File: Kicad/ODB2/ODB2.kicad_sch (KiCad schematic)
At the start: 31 parts, among them U1 STM32F412ZGTx

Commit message: ajout footprints
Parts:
- RST_C1: footprint (none) -> Capacitor_SMD:C_0805_2012Metric
- RST_R1: footprint (none) -> Resistor_SMD:R_0805_2012Metric
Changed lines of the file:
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@@
 			)
 		)
-		(property "Footprint" ""
+		(property "Footprint" "Resistor_SMD:R_0805_2012Metric"
 			(at 144.272 49.53 90)
 			(effects
@@
 			)
 		)
-		(property "Footprint" ""
+		(property "Footprint" "Capacitor_SMD:C_0805_2012Metric"
 			(at 147.0152 64.77 0)
 			(effects

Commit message: revision logic
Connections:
- net Pyros_DrogueOn renamed Pyros_DrogueODB
- net Pyros_MainOn renamed Pyros_MainODB
- net Pyros_Test renamed ~Pyros_Test

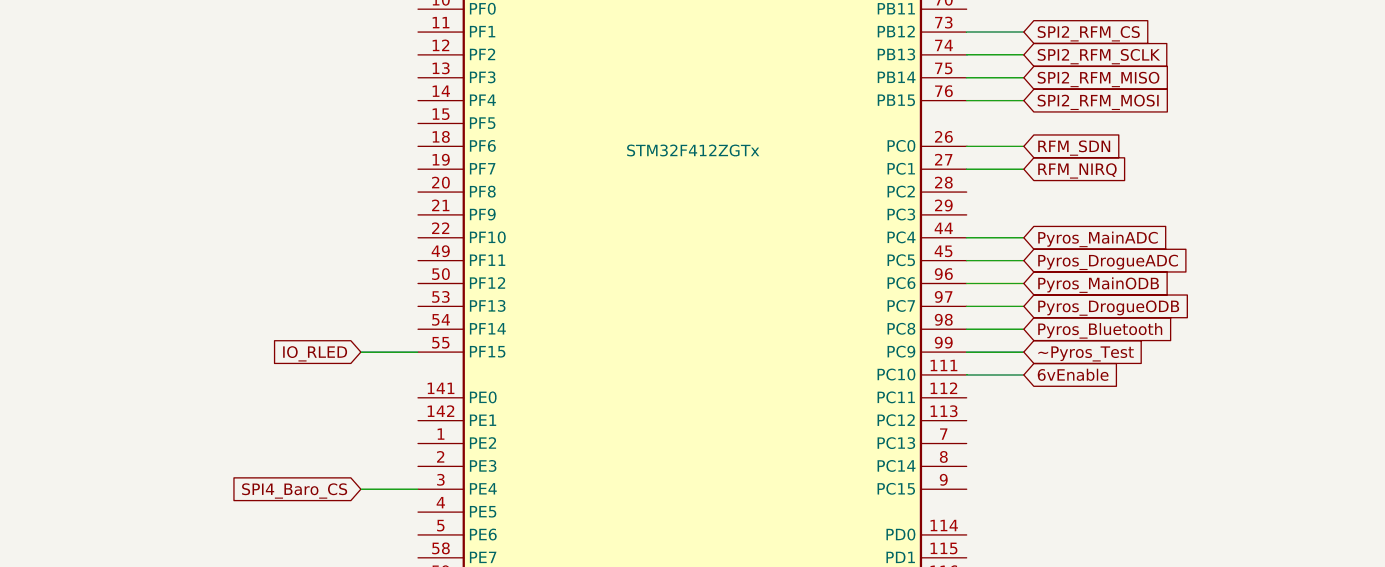
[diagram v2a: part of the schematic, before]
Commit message: ajout lecture tension batteries 1s / 2s
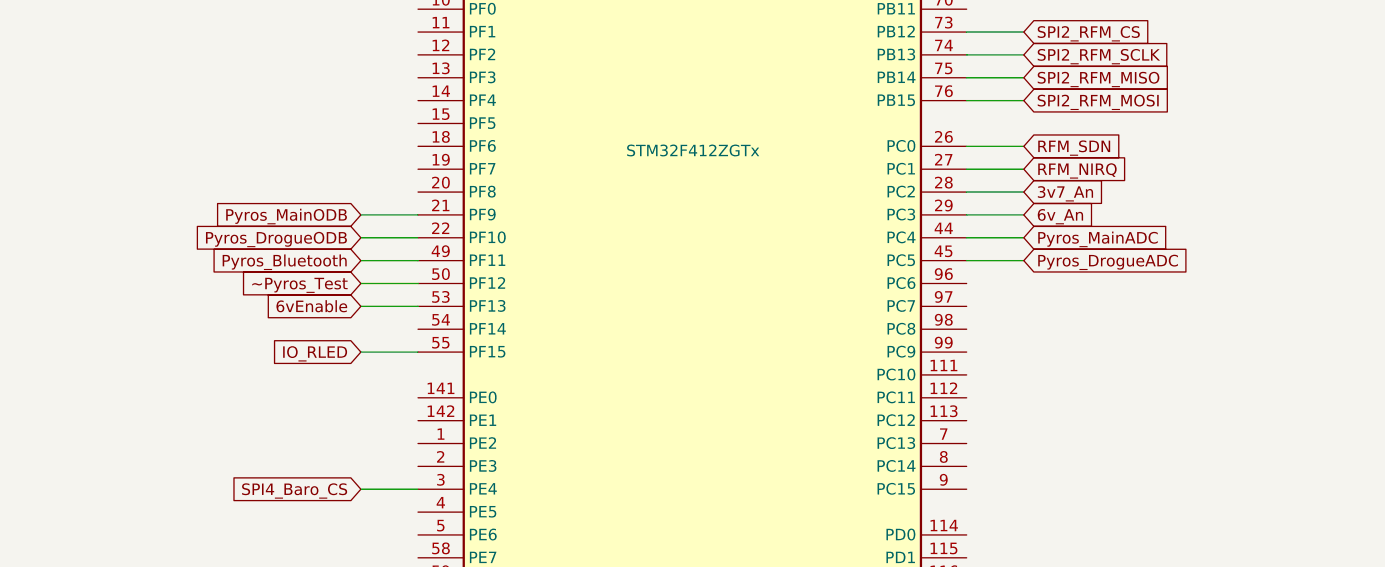
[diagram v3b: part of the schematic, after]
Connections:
- net 6vEnable: now also U1.53 (PF13); no longer U1.111 (PC10)
- net Pyros_Bluetooth: now also U1.49 (PF11); no longer U1.98 (PC8)
- net Pyros_DrogueODB: now also U1.22 (PF10); no longer U1.97 (PC7)
- net Pyros_MainODB: now also U1.21 (PF9); no longer U1.96 (PC6)
- net ~Pyros_Test: now also U1.50 (PF12); no longer U1.99 (PC9)
- net 3v7_An: now reaches U1.28 (PC2)
- net 6v_An: now reaches U1.29 (PC3)
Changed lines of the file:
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@@
-	(wire
-		(pts
-			(xy 231.14 162.56) (xy 237.49 162.56)
-		)
-		(stroke
-			(width 0)
-			(type default)
-		)
-	)
 	(wire
 		(pts
@@
 	(wire
 		(pts
+			(xy 231.14 149.86) (xy 237.49 149.86)
+		)
+		(stroke
+			(width 0)
+			(type default)
+		)
+	)
+	(wire
+		(pts
 			(xy 298.45 144.78) (xy 313.69 144.78)
 		)
@@
 	(wire
 		(pts
+			(xy 163.83 157.48) (xy 170.18 157.48)
+		)
+		(stroke
+			(width 0)
+			(type default)
+		)
+	)
+	(wire
+		(pts
 			(xy 375.92 139.7) (xy 375.92 142.24)
 		)
@@
 	(wire
 		(pts
+			(xy 231.14 147.32) (xy 237.49 147.32)
+		)
+		(stroke
+			(width 0)
+			(type default)
+		)
+	)
+	(wire
+		(pts
 			(xy 231.14 198.12) (xy 238.76 198.12)
 		)
@@
 	(wire
 		(pts
+			(xy 163.83 160.02) (xy 170.18 160.02)
+		)
+		(stroke
+			(width 0)
+			(type default)
+		)
+	)
+	(wire
+		(pts
 			(xy 163.83 180.34) (xy 170.18 180.34)
 		)
@@
 	(wire
 		(pts
-			(xy 231.14 160.02) (xy 237.49 160.02)
-		)
-		(stroke
-			(width 0)
-			(type default)
-		)
-	)
-	(wire
-		(pts
 			(xy 360.68 78.74) (xy 346.71 78.74)
 		)
@@
 	(wire
 		(pts
+			(xy 163.83 154.94) (xy 170.18 154.94)
+		)
+		(stroke
+			(width 0)
+			(type default)
+		)
+	)
+	(wire
+		(pts
 			(xy 388.62 31.75) (xy 392.43 31.75)
 		)
@@
 	(wire
 		(pts
-			(xy 231.14 165.1) (xy 237.49 165.1)
-		)
-		(stroke
-			(width 0)
-			(type default)
-		)
-	)
-	(wire
-		(pts
 			(xy 375.92 31.75) (xy 378.46 31.75)
 		)
@@
 	(wire
 		(pts
+			(xy 163.83 152.4) (xy 170.18 152.4)
+		)
+		(stroke
+			(width 0)
+			(type default)
+		)
+	)
+	(wire
+		(pts
 			(xy 360.68 66.04) (xy 346.71 66.04)
 		)
@@
 	(wire
 		(pts
+			(xy 163.83 149.86) (xy 170.18 149.86)
+		)
+		(stroke
+			(width 0)
+			(type default)
+		)
+	)
+	(wire
+		(pts
 			(xy 231.14 101.6) (xy 237.49 101.6)
 		)
@@
 	(wire
 		(pts
-			(xy 231.14 157.48) (xy 237.49 157.48)
-		)
-		(stroke
-			(width 0)
-			(type default)
-		)
-	)
-	(wire
-		(pts
 			(xy 300.99 88.9) (xy 316.23 88.9)
 		)
@@
 		(pts
 			(xy 316.23 99.06) (xy 316.23 101.6)
-		)
-		(stroke
-			(width 0)
-			(type default)
-		)
-	)
-	(wire
-		(pts
-			(xy 231.14 167.64) (xy 237.49 167.64)
 		)
 		(stroke
@@
 	(global_label "6vEnable"
 		(shape input)
-		(at 237.49 167.64 0)
-		(fields_autoplaced yes)
-		(effects
-			(font
-				(size 1.27 1.27)
-			)
-			(justify left)
-		)
-		(property "Intersheetrefs" "${INTERSHEET_REFS}"
-			(at 249.0021 167.64 0)
-			(effects
-				(font
-					(size 1.27 1.27)
-				)
-				(justify left)
+		(at 163.83 160.02 180)
+		(fields_autoplaced yes)
+		(effects
+			(font
+				(size 1.27 1.27)
+			)
+			(justify right)
+		)
+		(property "Intersheetrefs" "${INTERSHEET_REFS}"
+			(at 152.3179 160.02 0)
+			(effects
+				(font
+					(size 1.27 1.27)
+				)
+				(justify right)
 				(hide yes)
 			)
@@
 	(global_label "~Pyros_Test"
 		(shape input)
-		(at 237.49 165.1 0)
-		(fields_autoplaced yes)
-		(effects
-			(font
-				(size 1.27 1.27)
-			)
-			(justify left)
-		)
-		(property "Intersheetrefs" "${INTERSHEET_REFS}"
-			(at 251.3608 165.1 0)
-			(effects
-				(font
-					(size 1.27 1.27)
-				)
-				(justify left)
+		(at 163.83 157.48 180)
+		(fields_autoplaced yes)
+		(effects
+			(font
+				(size 1.27 1.27)
+			)
+			(justify right)
+		)
+		(property "Intersheetrefs" "${INTERSHEET_REFS}"
+			(at 149.9592 157.48 0)
+			(effects
+				(font
+					(size 1.27 1.27)
+				)
+				(justify right)
 				(hide yes)
 			)
@@
 		)
 	)
+	(global_label "3v7_An"
+		(shape input)
+		(at 237.49 147.32 0)
+		(fields_autoplaced yes)
+		(effects
+			(font
+				(size 1.27 1.27)
+			)
+			(justify left)
+		)
+		(property "Intersheetrefs" "${INTERSHEET_REFS}"
+			(at 247.067 147.32 0)
+			(effects
+				(font
+					(size 1.27 1.27)
+				)
+				(justify left)
+				(hide yes)
+			)
+		)
+	)
 	(global_label "SPI_ICM_CS"
 		(shape input)
@@
 	(global_label "Pyros_MainODB"
 		(shape input)
-		(at 237.49 157.48 0)
-		(fields_autoplaced yes)
-		(effects
-			(font
-				(size 1.27 1.27)
-			)
-			(justify left)
-		)
-		(property "Intersheetrefs" "${INTERSHEET_REFS}"
-			(at 254.8684 157.48 0)
+		(at 163.83 149.86 180)
+		(fields_autoplaced yes)
+		(effects
+			(font
+				(size 1.27 1.27)
+			)
+			(justify right)
+		)
+		(property "Intersheetrefs" "${INTERSHEET_REFS}"
+			(at 146.4516 149.86 0)
+			(effects
+				(font
+					(size 1.27 1.27)
+				)
+				(justify right)
+				(hide yes)
+			)
+		)
+	)
+	(global_label "6v_An"
+		(shape input)
+		(at 237.49 149.86 0)
+		(fields_autoplaced yes)
+		(effects
+			(font
+				(size 1.27 1.27)
+			)
+			(justify left)
+		)
+		(property "Intersheetrefs" "${INTERSHEET_REFS}"
+			(at 245.8575 149.86 0)
 			(effects
 				(font
@@
 	(global_label "Pyros_DrogueODB"
 		(shape input)
-		(at 237.49 160.02 0)
-		(fields_autoplaced yes)
-		(effects
-			(font
-				(size 1.27 1.27)
-			)
-			(justify left)
-		)
-		(property "Intersheetrefs" "${INTERSHEET_REFS}"
-			(at 257.106 160.02 0)
-			(effects
-				(font
-					(size 1.27 1.27)
-				)
-				(justify left)
+		(at 163.83 152.4 180)
+		(fields_autoplaced yes)
+		(effects
+			(font
+				(size 1.27 1.27)
+			)
+			(justify right)
+		)
+		(property "Intersheetrefs" "${INTERSHEET_REFS}"
+			(at 144.214 152.4 0)
+			(effects
+				(font
+					(size 1.27 1.27)
+				)
+				(justify right)
 				(hide yes)
 			)
@@
 	(global_label "Pyros_Bluetooth"
 		(shape input)
-		(at 237.49 162.56 0)
-		(fields_autoplaced yes)
-		(effects
-			(font
-				(size 1.27 1.27)
-			)
-			(justify left)
-		)
-		(property "Intersheetrefs" "${INTERSHEET_REFS}"
-			(at 255.7149 162.56 0)
-			(effects
-				(font
-					(size 1.27 1.27)
-				)
-				(justify left)
-				(hide yes)
-			)
+		(at 163.83 154.94 180)
+		(fields_autoplaced yes)
+		(effects
+			(font
+				(size 1.27 1.27)
+			)
+			(justify right)
+		)
+		(property "Intersheetrefs" "${INTERSHEET_REFS}"
+			(at 145.6051 154.94 0)
+			(effects
+				(font
+					(size 1.27 1.27)
+				)
+				(justify right)
+				(hide yes)
+			)

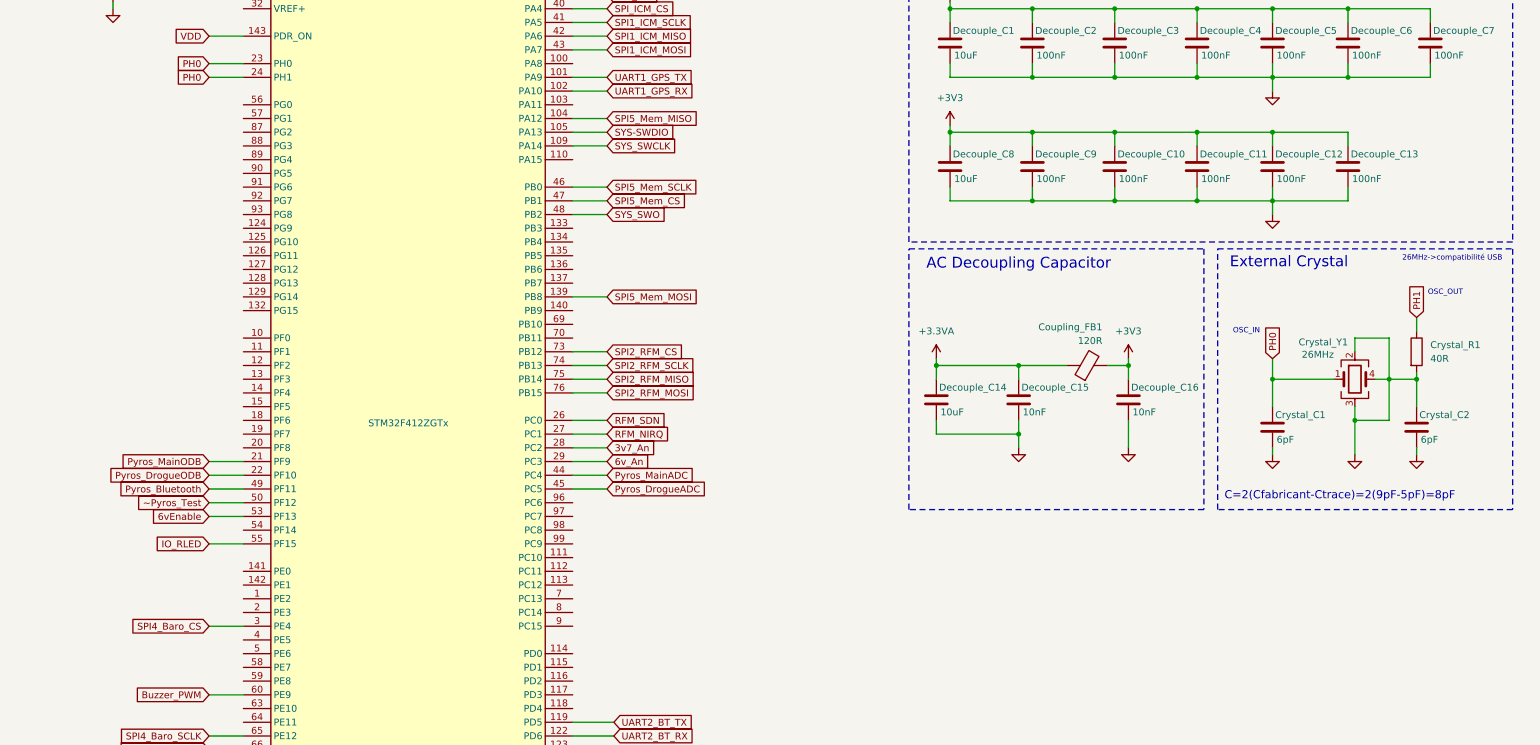
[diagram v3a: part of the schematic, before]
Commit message: ajout usbdata stm32 + modification pinout spi5_miso
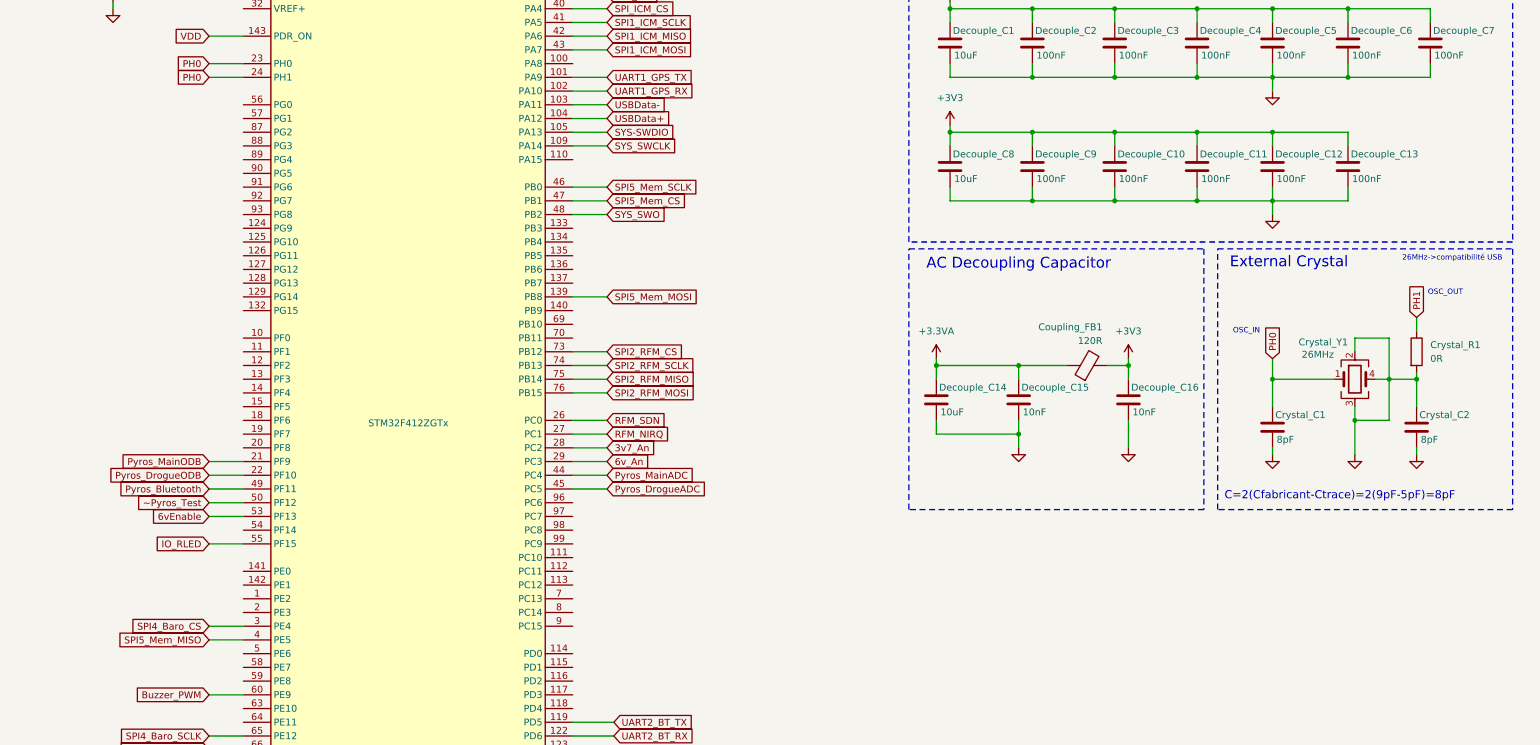
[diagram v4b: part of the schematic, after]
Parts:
- Crystal_C1, Crystal_C2: value 6pF -> 8pF
- Crystal_R1: value 40R -> 0R
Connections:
- net SPI5_Mem_MISO: now also U1.4 (PE5); no longer U1.104 (PA12)
- net USBData-: now reaches U1.103 (PA11)
- new net USBData+: U1.104 (PA12)
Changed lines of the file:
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@@
 	(wire
 		(pts
+			(xy 231.14 86.36) (xy 237.49 86.36)
+		)
+		(stroke
+			(width 0)
+			(type default)
+		)
+	)
+	(wire
+		(pts
 			(xy 360.68 88.9) (xy 346.71 88.9)
 		)
@@
 	(wire
 		(pts
+			(xy 231.14 83.82) (xy 237.49 83.82)
+		)
+		(stroke
+			(width 0)
+			(type default)
+		)
+	)
+	(wire
+		(pts
 			(xy 231.14 91.44) (xy 237.49 91.44)
 		)
@@
 	(wire
 		(pts
+			(xy 163.83 182.88) (xy 170.18 182.88)
+		)
+		(stroke
+			(width 0)
+			(type default)
+		)
+	)
+	(wire
+		(pts
 			(xy 139.7 55.88) (xy 146.05 55.88)
 		)
@@
 	(wire
 		(pts
-			(xy 231.14 86.36) (xy 237.49 86.36)
-		)
-		(stroke
-			(width 0)
-			(type default)
-		)
-	)
-	(wire
-		(pts
 			(xy 313.69 132.08) (xy 298.45 132.08)
 		)
@@
 	(global_label "SPI5_Mem_MISO"
 		(shape input)
-		(at 237.49 86.36 0)
+		(at 163.83 182.88 180)
 		(fields_autoplaced yes)
 		(effects
@@
 				(size 1.27 1.27)
 			)
-			(justify left)
+			(justify right)
 		)
 		(property "Intersheetrefs" "${INTERSHEET_REFS}"
-			(at 255.5337 86.36 0)
+			(at 145.7863 182.88 0)
 			(effects
 				(font
 					(size 1.27 1.27)
 				)
-				(justify left)
+				(justify right)
 				(hide yes)
 			)
@@
 		)
 	)
+	(global_label "USBData-"
+		(shape input)
+		(at 237.49 83.82 0)
+		(fields_autoplaced yes)
+		(effects
+			(font
+				(size 1.27 1.27)
+			)
+			(justify left)
+		)
+		(property "Intersheetrefs" "${INTERSHEET_REFS}"
+			(at 250.1513 83.82 0)
+			(effects
+				(font
+					(size 1.27 1.27)
+				)
+				(justify left)
+				(hide yes)
+			)
+		)
+	)
 	(global_label "SPI5_Mem_MOSI"
 		(shape input)
@@
 		)
 	)
+	(global_label "USBData+"
+		(shape input)
+		(at 237.49 86.36 0)
+		(fields_autoplaced yes)
+		(effects
+			(font
+				(size 1.27 1.27)
+			)
+			(justify left)
+		)
+		(property "Intersheetrefs" "${INTERSHEET_REFS}"
+			(at 250.1513 86.36 0)
+			(effects
+				(font
+					(size 1.27 1.27)
+				)
+				(justify left)
+				(hide yes)
+			)
+		)
+	)
 	(global_label "SYS_SWCLK"
 		(shape input)
@@
 			)
 		)
-		(property "Value" "6pF"
+		(property "Value" "8pF"
 			(at 361.442 145.796 0)
 			(effects
@@
 			)
 		)
-		(property "Value" "6pF"
+		(property "Value" "8pF"
 			(at 388.112 145.796 0)
 			(effects
@@
 			)
 		)
-		(property "Value" "40R"
+		(property "Value" "0R"
 			(at 389.89 130.8099 0)
 			(effects

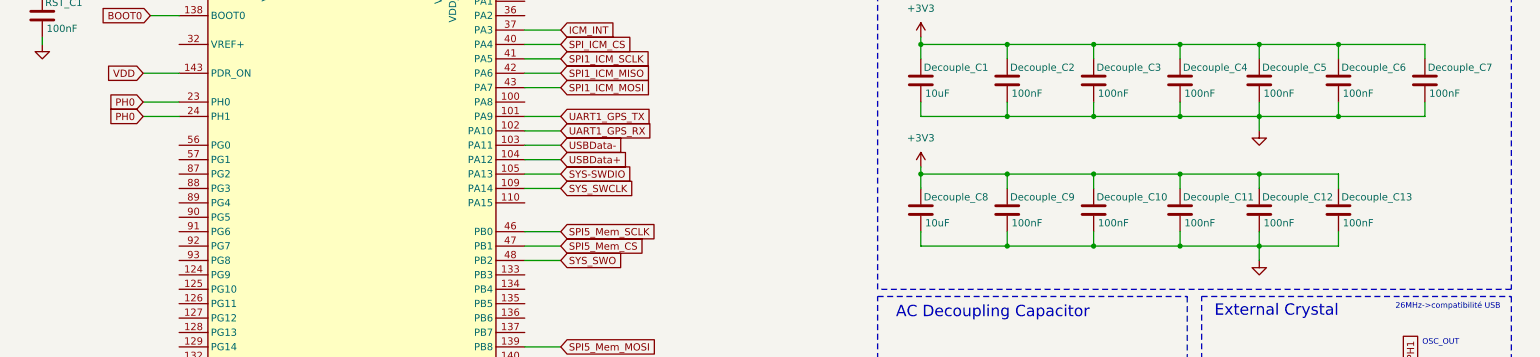
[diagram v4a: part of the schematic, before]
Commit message: fix label crystal + capacité découplage fix + add mosfet 6v isolation footprint
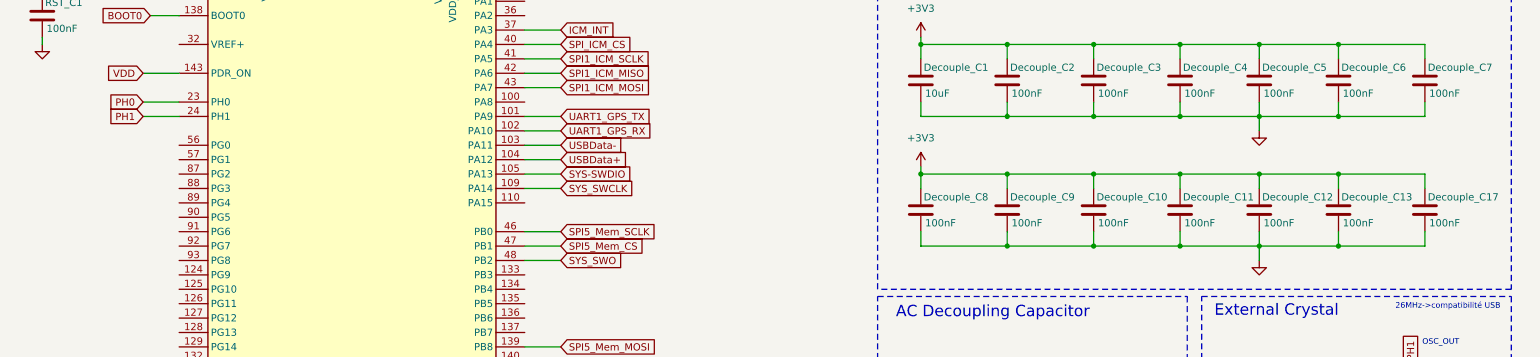
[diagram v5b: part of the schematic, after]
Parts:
- added Decouple_C17: 100nF, Capacitor_SMD:C_0805_2012Metric, symbol Device:C
- Decouple_C8: value 10uF -> 100nF
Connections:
- net +3V3: now also Decouple_C17.1
- net GND: now also Decouple_C17.2
- net PH0: no longer U1.24 (PH1)
- net PH1: now also U1.24 (PH1)
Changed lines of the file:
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@@
 	)
 	(junction
+		(at 374.65 88.9)
+		(diameter 0)
+		(color 0 0 0 0)
+	)
+	(junction
 		(at 387.35 134.62)
 		(diameter 0)
@@
 	)
 	(junction
+		(at 374.65 101.6)
+		(diameter 0)
+		(color 0 0 0 0)
+	)
+	(junction
 		(at 374.65 66.04)
 		(diameter 0)
@@
 	(wire
 		(pts
+			(xy 374.65 101.6) (xy 389.89 101.6)
+		)
+		(stroke
+			(width 0)
+			(type default)
+		)
+	)
+	(wire
+		(pts
 			(xy 213.36 44.45) (xy 210.82 44.45)
 		)
@@
 	(wire
 		(pts
+			(xy 389.89 99.06) (xy 389.89 101.6)
+		)
+		(stroke
+			(width 0)
+			(type default)
+		)
+	)
+	(wire
+		(pts
 			(xy 203.2 233.68) (xy 203.2 236.22)
 		)
@@
 	(wire
 		(pts
+			(xy 389.89 88.9) (xy 389.89 91.44)
+		)
+		(stroke
+			(width 0)
+			(type default)
+		)
+	)
+	(wire
+		(pts
 			(xy 163.83 154.94) (xy 170.18 154.94)
 		)
@@
 	(wire
 		(pts
+			(xy 374.65 88.9) (xy 389.89 88.9)
+		)
+		(stroke
+			(width 0)
+			(type default)
+		)
+	)
+	(wire
+		(pts
 			(xy 375.92 31.75) (xy 378.46 31.75)
 		)
@@
 		)
 	)
-	(global_label "PH0"
+	(global_label "PH1"
 		(shape input)
 		(at 163.83 78.74 180)
@@
 	)
 	(symbol
+		(lib_id "Device:C")
+		(at 389.89 95.25 0)
+		(unit 1)
+		(exclude_from_sim no)
+		(in_bom yes)
+		(on_board yes)
+		(dnp no)
+		(property "Reference" "Decouple_C17"
+			(at 390.398 92.964 0)
+			(effects
+				(font
+					(size 1.27 1.27)
+				)
+				(justify left)
+			)
+		)
+		(property "Value" "100nF"
+			(at 390.652 97.536 0)
+			(effects
+				(font
+					(size 1.27 1.27)
+				)
+				(justify left)
+			)
+		)
+		(property "Footprint" "Capacitor_SMD:C_0805_2012Metric"
+			(at 390.8552 99.06 0)
+			(effects
+				(font
+					(size 1.27 1.27)
+				)
+				(hide yes)
+			)
+		)
+		(property "Datasheet" "~"
+			(at 389.89 95.25 0)
+			(effects
+				(font
+					(size 1.27 1.27)
+				)
+				(hide yes)
+			)
+		)
+		(property "Description" "Unpolarized capacitor"
+			(at 389.89 95.25 0)
+			(effects
+				(font
+					(size 1.27 1.27)
+				)
+				(hide yes)
+			)
+		)
+		(pin "1"
+		)
+		(pin "2"
+		)
+		(instances
+			(project "ODB2"
+				(path "/4b06c5d1-aa8b-48ed-8972-b43a60cfab78"
+					(reference "Decouple_C17")
+					(unit 1)
+				)
+			)
+		)
+	)
+	(symbol
 		(lib_id "power:GND")
 		(at 334.01 147.32 0)
@@
 			)
 		)
-		(property "Value" "10uF"
+		(property "Value" "100nF"
 			(at 301.752 97.536 0)
 			(effects
